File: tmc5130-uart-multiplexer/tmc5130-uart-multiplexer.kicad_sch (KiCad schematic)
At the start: 0 parts

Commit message: tmc51x0-multiplexer-uart -> tmc5130-uart-multiplexer
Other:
- title: tmc51x0-multiplexer-uart -> tmc5130-uart-multiplexer
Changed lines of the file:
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@@
   (paper "A4")
   (title_block
-    (title "tmc51x0-multiplexer-uart")
+    (title "tmc5130-uart-multiplexer")
     (date "2024-07-10")
     (rev "1.0")
@@
     )
     (instances
-      (project "tmc51x0-multiplexer-uart"
+      (project "tmc5130-uart-multiplexer"
         (path "/df2b2e89-e055-4140-95de-f1df723db034" (page "2"))
       )
@@
     )
     (instances
-      (project "tmc51x0-multiplexer-uart"
+      (project "tmc5130-uart-multiplexer"
         (path "/df2b2e89-e055-4140-95de-f1df723db034" (page "5"))
       )
@@
     )
     (instances
-      (project "tmc51x0-multiplexer-uart"
+      (project "tmc5130-uart-multiplexer"
         (path "/df2b2e89-e055-4140-95de-f1df723db034" (page "9"))
       )
@@
     )
     (instances
-      (project "tmc51x0-multiplexer-uart"
+      (project "tmc5130-uart-multiplexer"
         (path "/df2b2e89-e055-4140-95de-f1df723db034" (page "11"))
       )
@@
     )
     (instances
-      (project "tmc51x0-multiplexer-uart"
+      (project "tmc5130-uart-multiplexer"
         (path "/df2b2e89-e055-4140-95de-f1df723db034" (page "4"))
       )
@@
     )
     (instances
-      (project "tmc51x0-multiplexer-uart"
+      (project "tmc5130-uart-multiplexer"
         (path "/df2b2e89-e055-4140-95de-f1df723db034" (page "7"))
       )
@@
     )
     (instances
-      (project "tmc51x0-multiplexer-uart"
+      (project "tmc5130-uart-multiplexer"
         (path "/df2b2e89-e055-4140-95de-f1df723db034" (page "6"))
       )
@@
     )
     (instances
-      (project "tmc51x0-multiplexer-uart"
+      (project "tmc5130-uart-multiplexer"
         (path "/df2b2e89-e055-4140-95de-f1df723db034" (page "10"))
       )
@@
     )
     (instances
-      (project "tmc51x0-multiplexer-uart"
+      (project "tmc5130-uart-multiplexer"
         (path "/df2b2e89-e055-4140-95de-f1df723db034" (page "3"))
       )
@@
     )
     (instances
-      (project "tmc51x0-multiplexer-uart"
+      (project "tmc5130-uart-multiplexer"
         (path "/df2b2e89-e055-4140-95de-f1df723db034" (page "8"))
       )

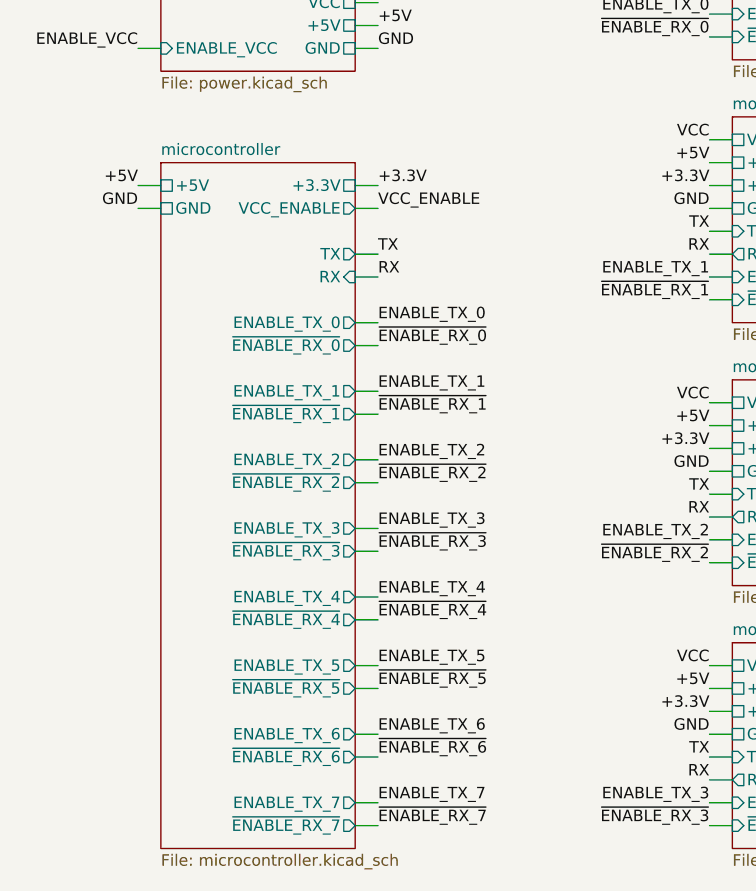
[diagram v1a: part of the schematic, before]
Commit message: Fix some design rule checks
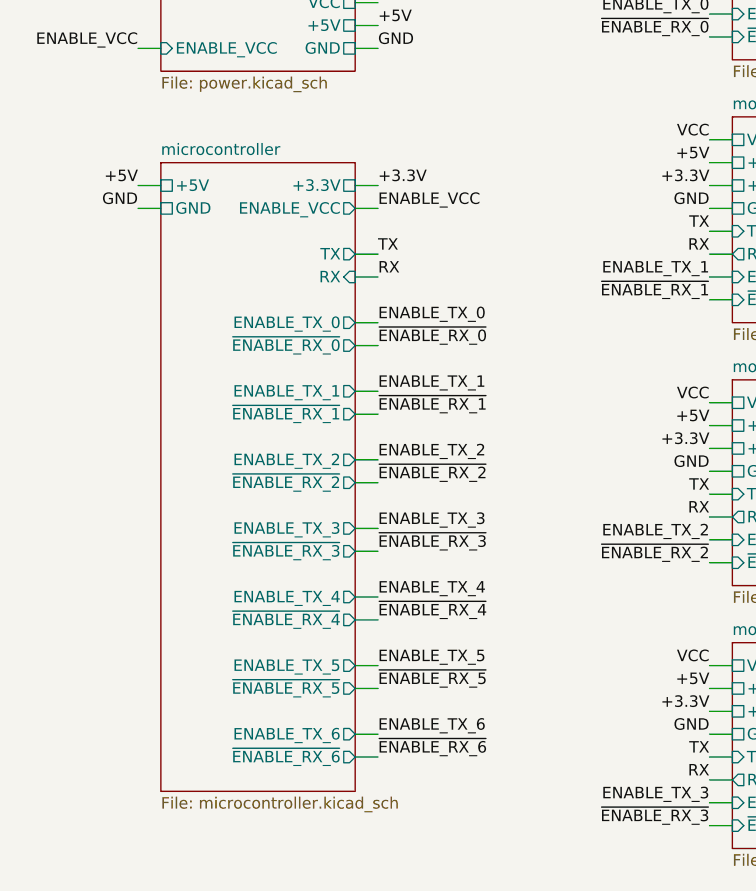
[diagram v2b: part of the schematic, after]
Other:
- sheet microcontroller ports: added ENABLE_VCC; removed ENABLE_TX_7, VCC_ENABLE, ~{ENABLE_RX_7}
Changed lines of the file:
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@@
-    (stroke (width 0) (type default))
-  )
-  (wire (pts (xy 93.98 154.94) (xy 96.52 154.94))
     (stroke (width 0) (type default))
   )
@@
     (stroke (width 0) (type default))
   )
-  (wire (pts (xy 93.98 157.48) (xy 96.52 157.48))
-    (stroke (width 0) (type default))
-  )
   (wire (pts (xy 133.35 83.82) (xy 135.89 83.82))
     (stroke (width 0) (type default))
@@
     (effects (font (size 1.27 1.27)) (justify left bottom))
   )
-  (label "VCC_ENABLE" (at 96.52 88.9 0) (fields_autoplaced)
+  (label "ENABLE_VCC" (at 96.52 88.9 0) (fields_autoplaced)
     (effects (font (size 1.27 1.27)) (justify left bottom))
   )
@@
     (effects (font (size 1.27 1.27)) (justify left bottom))
   )
-  (label "~{ENABLE_RX_7}" (at 96.52 157.48 0) (fields_autoplaced)
-    (effects (font (size 1.27 1.27)) (justify left bottom))
-  )
   (label "~{ENABLE_RX_6}" (at 179.07 128.27 180) (fields_autoplaced)
     (effects (font (size 1.27 1.27)) (justify right bottom))
-  )
-  (label "ENABLE_TX_7" (at 96.52 154.94 0) (fields_autoplaced)
-    (effects (font (size 1.27 1.27)) (justify left bottom))
   )
   (label "TX" (at 179.07 91.44 180) (fields_autoplaced)
@@
     )
   )
-  (sheet (at 72.39 83.82) (size 21.59 76.2) (fields_autoplaced)
+  (sheet (at 72.39 83.82) (size 21.59 69.85) (fields_autoplaced)
     (stroke (width 0.1524) (type solid))
     (fill (color 0 0 0 0.0000))
@@
       (effects (font (size 1.27 1.27)) (justify left bottom))
     )
-    (property "Sheetfile" "microcontroller.kicad_sch" (at 72.39 160.6046 0)
+    (property "Sheetfile" "microcontroller.kicad_sch" (at 72.39 154.2546 0)
       (effects (font (size 1.27 1.27)) (justify left top))
     )
@@
       (effects (font (size 1.27 1.27)) (justify right))
     )
-    (pin "ENABLE_TX_7" output (at 93.98 154.94 0)
-      (effects (font (size 1.27 1.27)) (justify right))
-    )
-    (pin "VCC_ENABLE" output (at 93.98 88.9 0)
-      (effects (font (size 1.27 1.27)) (justify right))
-    )
-    (pin "~{ENABLE_RX_7}" output (at 93.98 157.48 0)
-      (effects (font (size 1.27 1.27)) (justify right))
-    )
+    (pin "ENABLE_VCC" output (at 93.98 88.9 0)
+      (effects (font (size 1.27 1.27)) (justify right))
+    )
